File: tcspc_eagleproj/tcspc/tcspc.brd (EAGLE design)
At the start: 100 x 50 mm, 1 part, among them U1 THS788

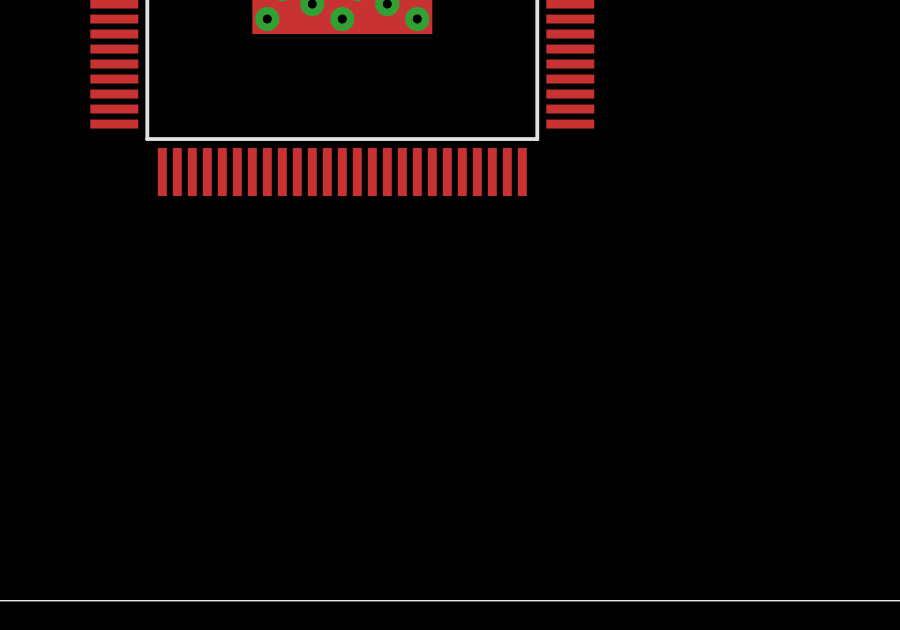
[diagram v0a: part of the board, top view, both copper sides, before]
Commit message: added the SiT5021 Oscillator to the library
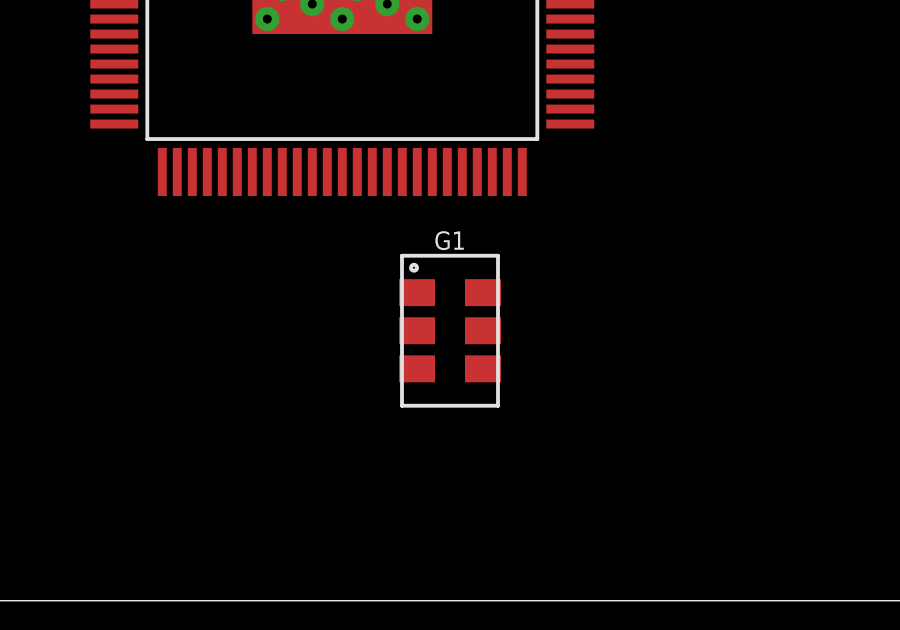
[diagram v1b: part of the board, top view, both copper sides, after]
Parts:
- added G1: 200MHz, tcspc_lib:SIT5021_5X3.2
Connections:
- new net N$1: G1.5, U1.20
- new net N$2: G1.4, U1.19
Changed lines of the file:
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@@
 <elements>
 <element name="U1" library="tcspc_lib" package="S-PQFP-G100" value="THS788" x="50.41" y="21.89"/>
+<element name="G1" library="tcspc_lib" package="SIT5021_5X3.2" value="200MHz" x="54" y="9" rot="R270"/>
 </elements>
 <signals>
@@
 <wire x1="58.01" y1="23.89" x2="58.01" y2="22.39" width="0" layer="19" extent="1-1"/>
 </signal>
+<signal name="N$1">
+<contactref element="G1" pad="5"/>
+<contactref element="U1" pad="20"/>
+<wire x1="55.1" y1="9" x2="53.91" y2="14.29" width="0" layer="19" extent="1-1"/>
+</signal>
+<signal name="N$2">
+<contactref element="U1" pad="19"/>
+<contactref element="G1" pad="4"/>
+<wire x1="55.1" y1="7.73" x2="53.41" y2="14.29" width="0" layer="19" extent="1-1"/>
+</signal>
 </signals>

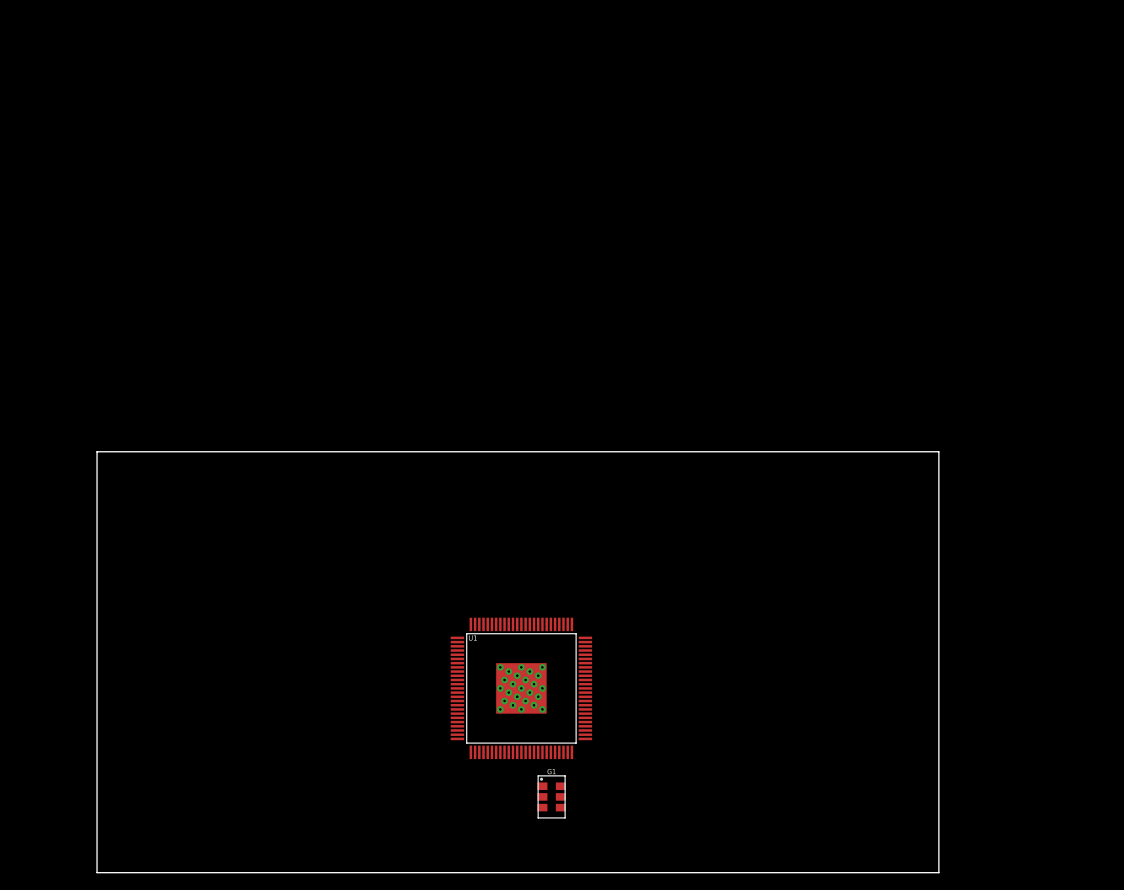
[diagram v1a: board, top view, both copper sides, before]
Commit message: threw a couple SMAs and DACs onto the schematic
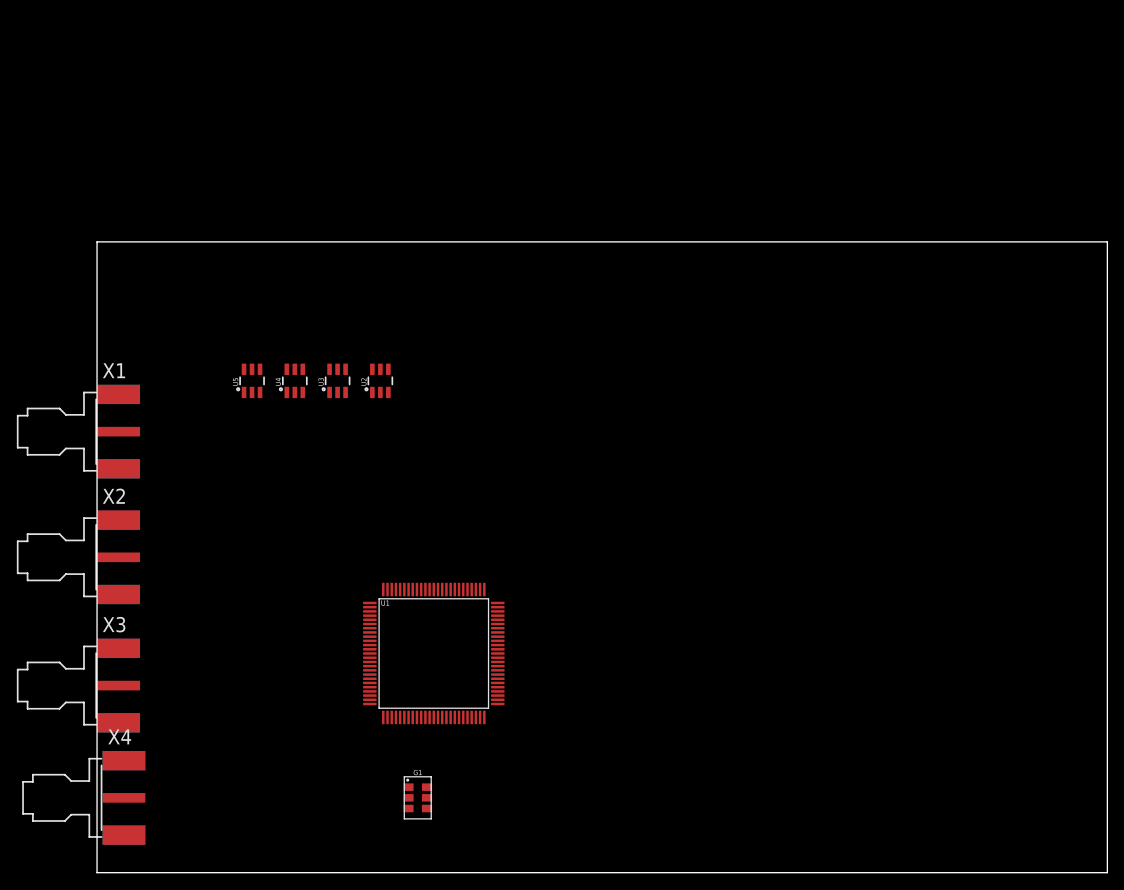
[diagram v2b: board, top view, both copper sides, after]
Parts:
- added U2, U3, U4, U5: MCP4725, tcspc_lib:SOT23-6
- added X1, X2, X3, X4: SMA, tcspc_lib:J502-ND-142-0701-881/886
- U1: device tcspc_lib:S-PQFP-G100 -> tcspc_lib:S-QFP-G100
- moved G1 15.9 mm to (38.1, 8.89)
- moved U1 11.2 mm to (40.0, 26.0)
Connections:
- net GND: now also X1.G@1, X1.G@2, X1.G@3, X1.G@4, X2.G@1, X2.G@2, X2.G@3, X2.G@4, X3.G@1, X3.G@2, X3.G@3, X3.G@4, X4.G@1, X4.G@2, X4.G@3, X4.G@4
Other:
- board size 100 x 50 mm -> 120 x 74.9 mm

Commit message: Added 0402 option to the library, tweaked the front end, organized and ordered the front end on the board, added a bunch of bypass caps for the TDC.
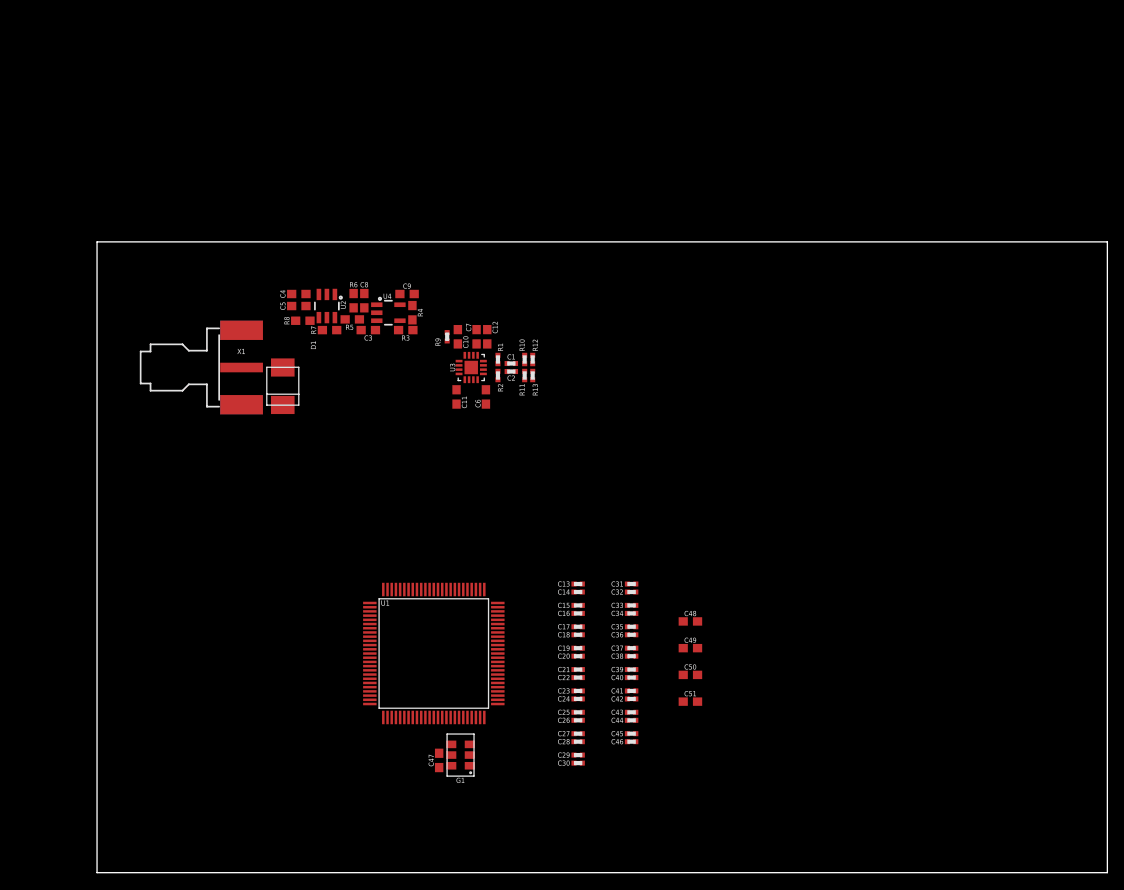
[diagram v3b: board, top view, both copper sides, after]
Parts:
- removed U5: MCP4725, tcspc_lib:SOT23-6
- removed X2, X3, X4: SMA, tcspc_lib:J502-ND-142-0701-881/886
- added C1, C2: 10pF, tcspc_lib:0402
- added C10, C11, C12, C3, C4, C47, C6, C7, C8, C9: .1uF, tcspc_lib:0603
- added C13, C15, C17, C19, C21, C23, C25, C27, C29, C31, C33, C35, C37, C39, C41, C43, C45: .1uF, tcspc_lib:0402
- added C14, C16, C18, C20, C22, C24, C26, C28, C30, C32, C34, C36, C38, C40, C42, C44, C46: 10nF, tcspc_lib:0402
- added C48, C49, C50, C51: 1uF, tcspc_lib:0603
- added C5: 10uF, tcspc_lib:0603
- added D1: 3.3V, tcspc_lib:DO-214AA
- added R1, R2: 50, tcspc_lib:0402
- added R10, R11, R12, R13: (no value), tcspc_lib:0402
- added R3, R4, R5: 1k, tcspc_lib:0603
- added R6: 0, tcspc_lib:0603
- added R7, R8: 2.2k, tcspc_lib:0603
- added R9: 0, tcspc_lib:0402
- U3: value MCP4725 -> ADCMP582; device tcspc_lib:SOT23-6 -> tcspc_lib:QFN50P300X300X80-16N
- U4: value MCP4725 -> LT6003_SOT23-5; device tcspc_lib:SOT23-6 -> tcspc_lib:SOT23-5
- moved X1 16.5 mm to (14.6, 60.0)
- moved U3 16.0 mm to (44.5, 60.0)
- moved U4 13.7 mm to (34.6, 66.5), turned to 270 degrees
- moved U2 10.9 mm to (27.3, 67.3), turned to 180 degrees
- moved G1 7.18 mm to (43.2, 14.0), turned to 90 degrees
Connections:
- removed net VCC: U1.16, U1.22, U1.23, U1.24, U1.31, U1.36, U1.38, U1.40, U1.43, U1.58, U1.60, U1.69, U1.7, U1.77, U1.83, U1.86, U1.88, U1.90, U1.91, U1.93, U1.99
- new net !TMU_DOUT_A: U1.79
- new net !TMU_IN_A: U1.66
- new net !TMU_IN_B: U1.63
- new net !TMU_IN_C: U1.10
- new net !TMU_IN_D: U1.13
- new net N$10: U1.52
- new net N$11: U1.53
- new net N$12: R3.1, R4.2, U4.4
- new net N$13: R3.2, U3.2, U4.1
- new net N$14: U1.51
- new net N$15: U1.33
- new net N$16: U1.34
- new net N$17: U1.41
- new net N$18: D1.A, U3.3, X1.1
- new net N$19: R7.2, U2.5
- new net N$20: R8.2, U2.4
- new net N$21: U1.30
- new net N$22: U1.29
- new net N$23: U1.95
- new net N$24: U1.96
- new net N$25: U1.46
- new net N$26: U1.47
- new net N$27: U1.81
- new net N$28: U1.80
- new net N$29: U1.44
- new net N$3: C2.1, R2.1, U3.10
- new net N$30: U1.45
- new net N$31: U1.28
- new net N$32: U1.27
- new net N$33: U1.97
- new net N$34: U1.98
- new net N$35: U1.48
- new net N$36: U1.49
- new net N$4: C1.2, R10.2, R12.1
- new net N$5: C2.2, R11.2, R13.1
- new net N$6: C1.1, R1.1, U3.11
- new net N$7: R9.2, U3.1
- new net N$8: R6.1, U2.1
- new net N$9: C3.1, R5.1, R6.2, U4.3
- new net PP_N3V3: C7.1, C8.1, U3.13, U4.2
- new net PP_P3V3: C10.1, C11.1, C12.1, C13.1, C14.1, C15.1, C16.1, C17.1, C18.1, C19.1, C20.1, C21.1, C22.1, C23.1, C24.1, C25.1, C26.1, C27.1, C28.1, C29.1, C30.1, C31.1, C32.1, C33.1, C34.1, C35.1, C36.1, C37.1, C38.1, C39.1, C4.1, C40.1, C41.1, C42.1, C43.1, C44.1, C45.1, C46.1, C47.1, C48.1, C49.1, C5.1, C50.1, C51.1, C6.1, C9.1, G1.6, R10.1, R11.1, R4.1, R7.1, R8.1, U1.16, U1.22, U1.23, U1.24, U1.31, U1.36, U1.38, U1.40, U1.43, U1.58, U1.60, U1.69, U1.7, U1.77, U1.83, U1.86, U1.88, U1.90, U1.91, U1.93, U1.99, U2.3, U3.12, U3.16, U3.5, U3.9, U4.5
- new net TMU_DOUT_A: U1.78
- new net TMU_IN_A: U1.68
- new net TMU_IN_B: U1.61
- new net TMU_IN_C: U1.8
- new net TMU_IN_D: U1.15
- net GND: now also C10.2, C11.2, C12.2, C13.2, C14.2, C15.2, C16.2, C17.2, C18.2, C19.2, C20.2, C21.2, C22.2, C23.2, C24.2, C25.2, C26.2, C27.2, C28.2, C29.2, C3.2, C30.2, C31.2, C32.2, C33.2, C34.2, C35.2, C36.2, C37.2, C38.2, C39.2, C4.2, C40.2, C41.2, C42.2, C43.2, C44.2, C45.2, C46.2, C47.2, C48.2, C49.2, C5.2, C50.2, C51.2, C6.2, C7.2, C8.2, C9.2, D1.C, G1.3, R1.2, R12.2, R13.2, R2.2, R5.2, R9.1, U2.2, U2.6, U3.14, U3.15, U3.4; no longer X2.G@1, X2.G@2, X2.G@3, X2.G@4, X3.G@1, X3.G@2, X3.G@3, X3.G@4, X4.G@1, X4.G@2, X4.G@3, X4.G@4

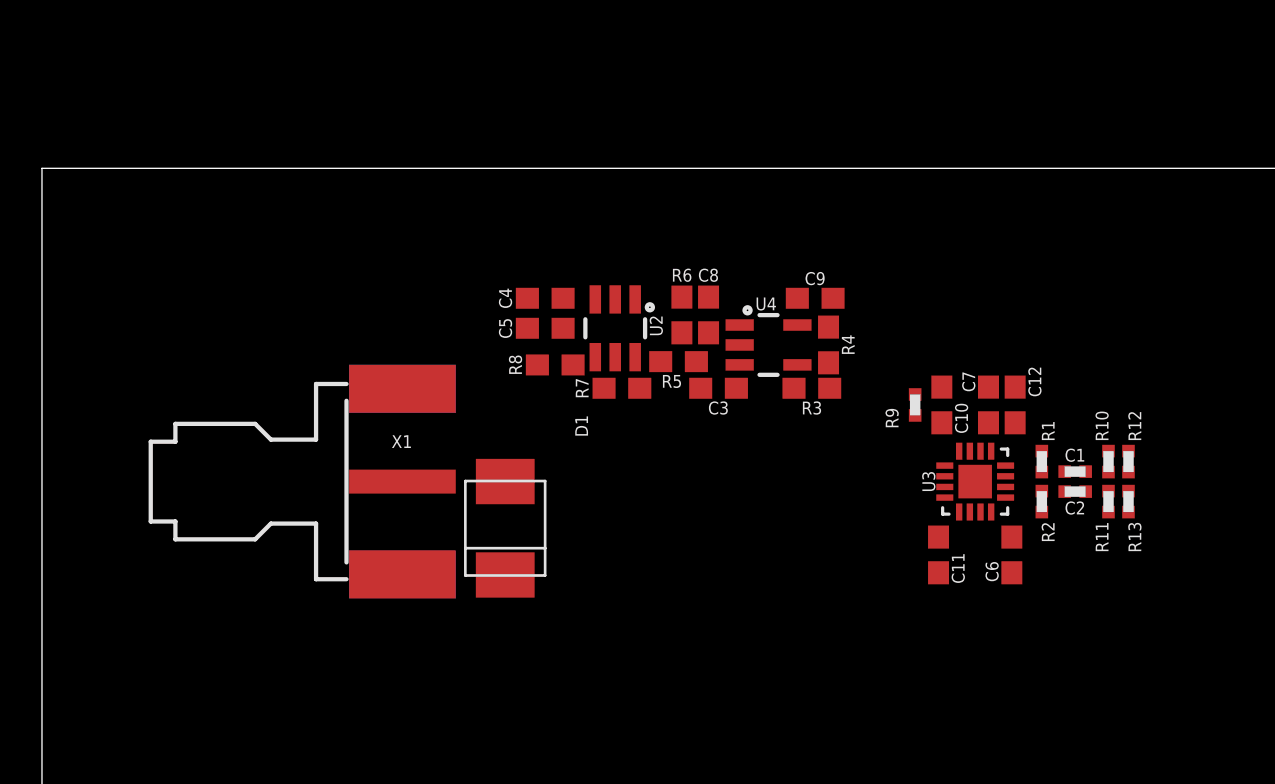
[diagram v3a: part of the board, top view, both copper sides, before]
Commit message: Modified the 0402 package to have layout indicators, so I can leave myself some room for when I assemble the board. Twiddled the layout of the frontend, so that I can try get a frontend demo board out the door.
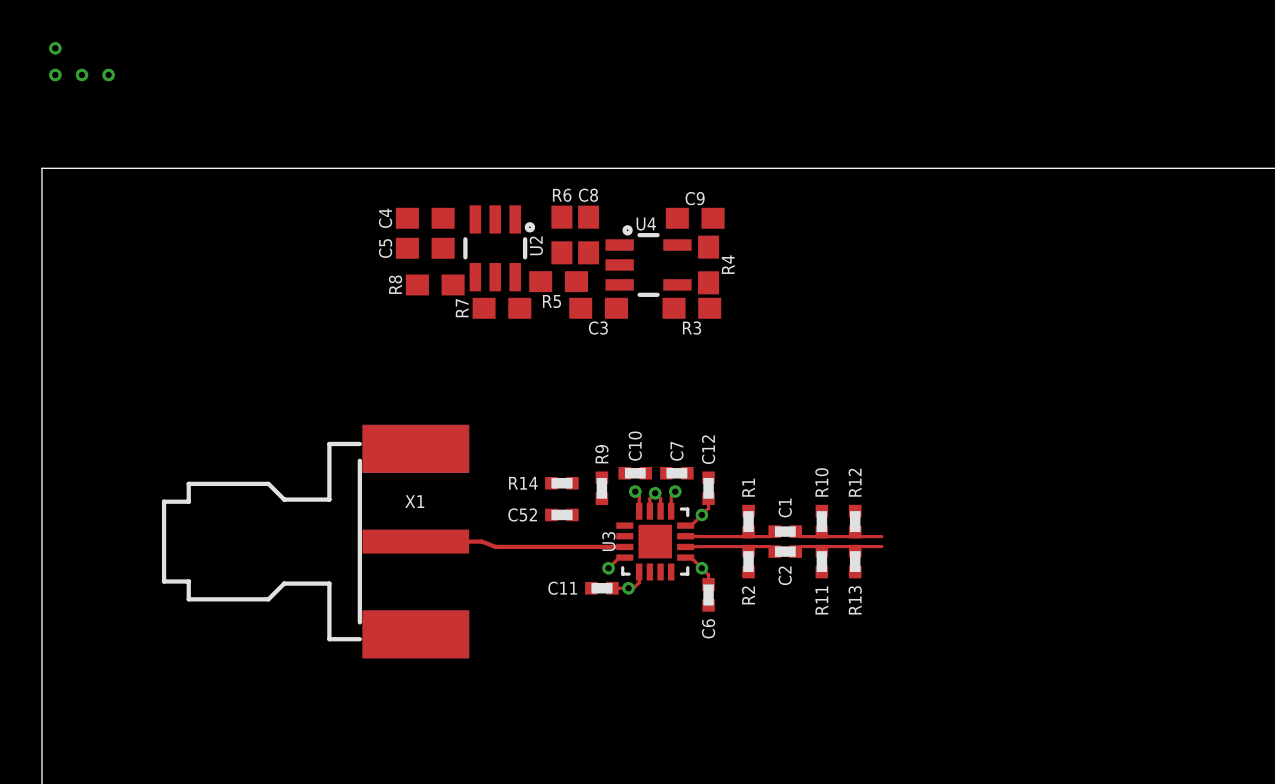
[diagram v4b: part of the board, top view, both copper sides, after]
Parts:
- removed D1: 3.3V, tcspc_lib:DO-214AA
- added C52: 10nF, tcspc_lib:0402
- added R14: 0, tcspc_lib:0402
- C10, C11, C12, C6, C7: device tcspc_lib:0603 -> tcspc_lib:0402
- moved C11 16.1 mm to (26.7, 54.9), turned to 180 degrees
- moved U3 15.5 mm to (29.2, 57.1)
- moved R9 15.4 mm to (26.7, 59.7)
- moved C7 15.2 mm to (30.2, 60.4), turned to 180 degrees
- moved C12 15.1 mm to (31.8, 59.7)
- moved C10 15.0 mm to (28.3, 60.4), turned to 0 degrees
- moved C6 14.6 mm to (31.8, 54.6)
- moved R1 14.3 mm to (33.7, 58.1)
- moved R2 14.3 mm to (33.7, 56.2)
- moved C1 14.1 mm to (35.4, 57.6)
- moved C2 14.1 mm to (35.4, 56.7)
- moved R10 13.9 mm to (37.1, 58.1)
- moved R11 13.9 mm to (37.1, 56.2)
- moved R12 13.3 mm to (38.7, 58.1)
- moved R13 13.3 mm to (38.7, 56.2)
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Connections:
- new net N$37: C52.2, R14.2, U3.2
- net GND: now also C52.1; no longer D1.C
- net N$13: now also R14.1; no longer U3.2
- net N$18: no longer D1.A
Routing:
- net N$18: track 0.00 -> 10.0 mm
- net PP_P3V3: track 0.00 -> 6.68 mm, vias 0 -> 5
- net N$5: track 0.00 -> 4.63 mm
- net N$4: track 0.00 -> 4.63 mm
- net N$3: track 0.00 -> 4.56 mm
- net N$6: track 0.00 -> 4.56 mm
- net GND: track 0.00 -> 2.90 mm, vias 0 -> 3
- net PP_N3V3: track 0.00 -> 0.74 mm, vias 0 -> 2

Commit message: not 100% sure what changes got made here but there was a good chunk of progress nonetheless
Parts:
- added C53, C54, C55: .1uF, tcspc_lib:0402
- added Q1: (no value), jack_semi:SOT23-3
- added R15: 210, tcspc_lib:0402
- added R16: 100, tcspc_lib:0402
- added R17, R18, R19, R20, R21, R22, R23: DNP, tcspc_lib:0402
- added U5: LT6003_SOT23-5, tcspc_lib:SOT23-5
- C3, C4, C5, C8, C9, R3, R4, R5, R6, R7, R8: device tcspc_lib:0603 -> tcspc_lib:0402
- moved C7 0.08 mm to (30.2, 60.4), turned to 0 degrees
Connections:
- removed net PP_N3V3: C7.1, C8.1, U3.13, U4.2
- new net N$38: R17.2, R18.1, U3.8
- new net N$39: R15.1, R19.2, U3.7
- new net N$41: R16.2, R20.1, U3.6
- new net N$42: Q1.3, U3.14
- new net N$43: Q1.1, U5.1
- new net N$45: C55.1, R22.2, R23.1, U5.4
- new net N$46: R22.1
- new net N$47: Q1.2, R21.1, R23.2
- new net PP_N3V3_ANALOG: C53.1, C7.2, C8.1, R21.2, U3.13, U4.2, U5.2
- new net PP_P3V3_ANALOG: C10.1, C11.1, C4.1, C5.1, C54.1, C6.1, C9.1, R4.1, R7.1, R8.1, U2.3, U3.16, U3.5, U4.5, U5.5
- new net PP_P3V3_DIGITAL: C12.1, R10.1, R11.1, R16.1, R17.1, R19.1, U3.12, U3.9
- net GND: now also C53.2, C54.2, C55.2, C7.1, R15.2, R18.2, R20.2, U5.3; no longer C7.2, U3.14
- net PP_P3V3: no longer C10.1, C11.1, C12.1, C4.1, C5.1, C6.1, C9.1, R10.1, R11.1, R4.1, R7.1, R8.1, U2.3, U3.12, U3.16, U3.5, U3.9, U4.5
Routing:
- net PP_P3V3: track 6.68 -> 0.00 mm, vias 5 -> 1
- net PP_P3V3_ANALOG: track 0.00 -> 4.53 mm, vias 0 -> 3
- net GND: track 2.90 -> 0.99 mm, vias 3 -> 2
- net PP_P3V3_DIGITAL: track 0.00 -> 1.89 mm, vias 0 -> 1
- net PP_N3V3_ANALOG: track 0.00 -> 0.74 mm, vias 0 -> 2
- net PP_N3V3: track 0.74 -> 0.00 mm, vias 2 -> 0
